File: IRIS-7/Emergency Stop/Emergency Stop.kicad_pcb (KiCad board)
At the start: 2 copper layers, 40 x 50 mm, 36 parts, among them IC1 LMR16006, J1 5mm TB, J2 ESTOP, J3 Pwr, J4 5mm TB, Q1 BSS123, Q2 BSS123, Q3 DMP3099L

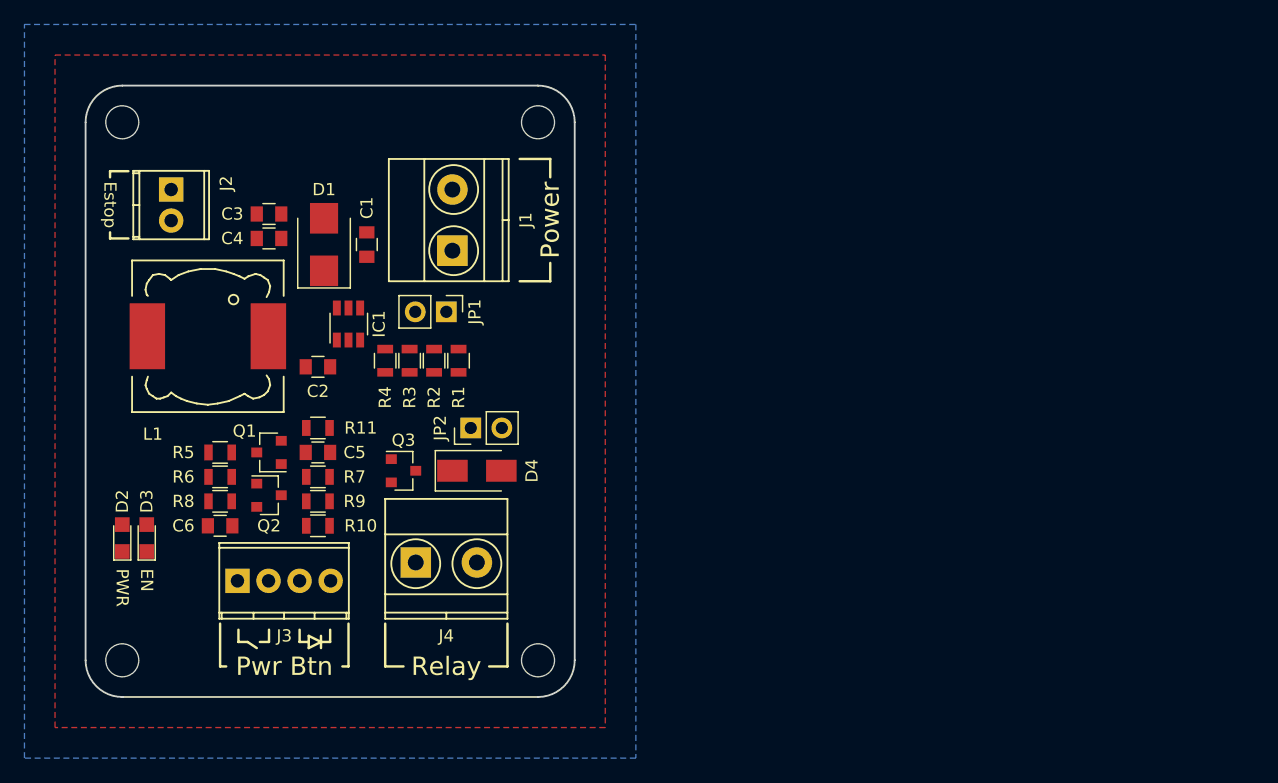
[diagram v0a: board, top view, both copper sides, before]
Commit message: Complete most of the routing
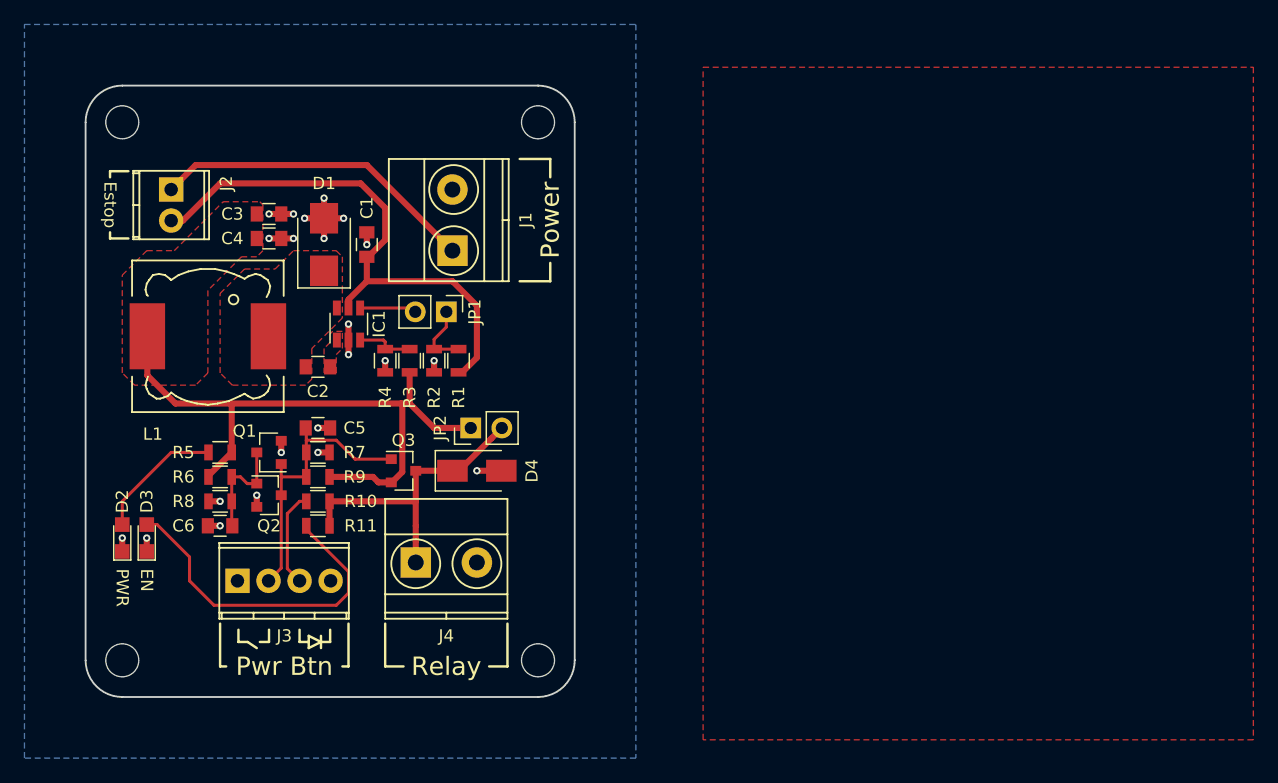
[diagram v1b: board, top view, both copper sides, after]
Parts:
- moved R11 8.00 mm to (119.0, 86.0)
- moved C5 2.00 mm to (119.0, 78.0)
- moved R10 2.00 mm to (119.0, 84.0)
- moved R7 2.00 mm to (119.0, 80.0)
- moved R9 2.00 mm to (119.0, 82.0)
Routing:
- net +12V: track 0.00 -> 54.0 mm
- net /Vin: track 0.00 -> 45.2 mm
- net Net-(D3-Pad2): track 0.00 -> 27.7 mm
- net /Vbatt: track 0.00 -> 26.7 mm
- net GND: track 0.00 -> 25.9 mm, vias 0 -> 22
- net /12Vout: track 0.00 -> 25.0 mm
- net /~EN: track 0.00 -> 23.7 mm
- net Net-(D2-Pad2): track 0.00 -> 10.6 mm
- net Net-(J3-Pad3): track 0.00 -> 8.96 mm
- net /EN: track 0.00 -> 8.85 mm
- net /UVLO: track 0.00 -> 5.46 mm
- net /FB: track 0.00 -> 4.71 mm
- net /~SHDN: track 0.00 -> 4.64 mm
- added copper zone on F.Cu, net +12V
- added copper zone on F.Cu, net /BOOT
- added copper zone on F.Cu, net /SW

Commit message: Clean up copper zones
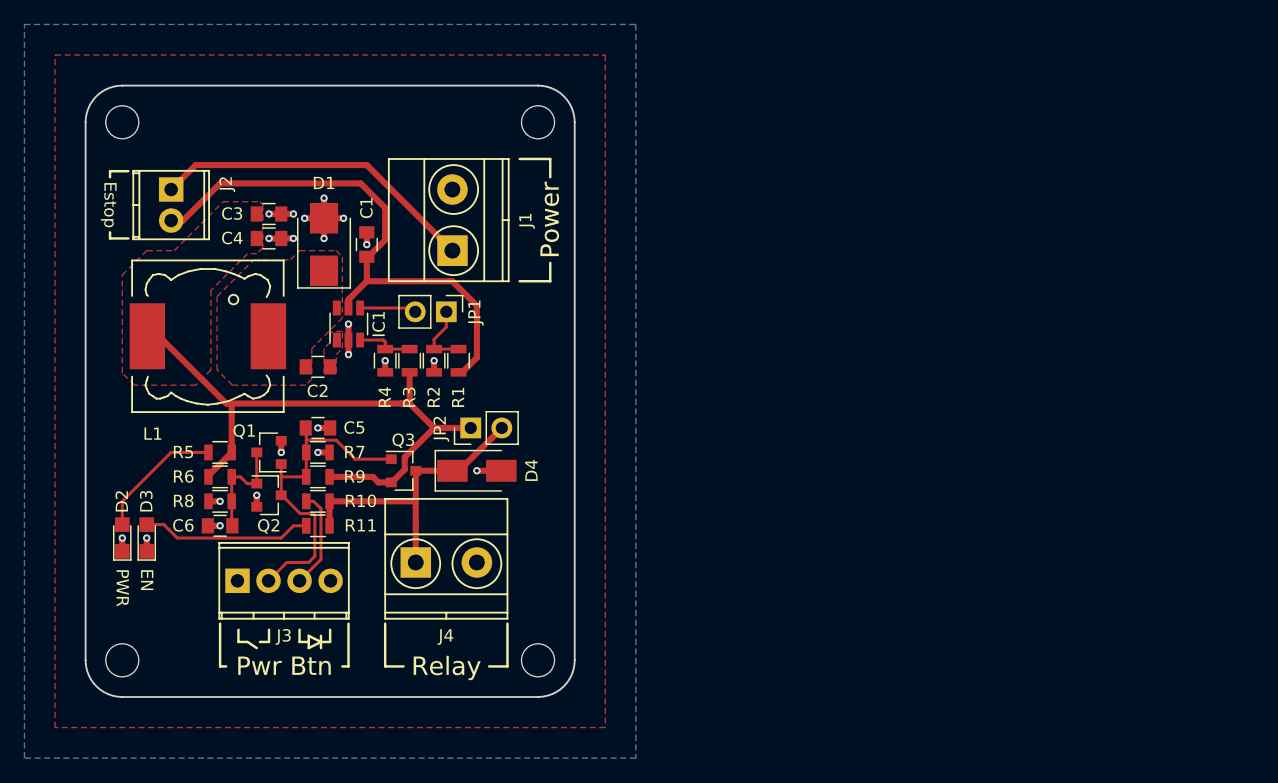
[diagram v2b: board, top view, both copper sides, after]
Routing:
- net Net-(D3-Pad2): track 27.7 -> 14.2 mm
- net /~EN: track 23.7 -> 27.6 mm
- net +12V: track 54.0 -> 51.1 mm
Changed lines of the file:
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@@
   (general
     (links 58)
-    (no_connects 48)
+    (no_connects 0)
     (area 99.924999 49.924999 140.075001 100.075001)
     (thickness 1.6)
     (drawings 43)
-    (tracks 140)
+    (tracks 142)
     (zones 0)
     (modules 36)
@@
   (layers
     (0 F.Cu signal)
-    (31 B.Cu signal hide)
+    (31 B.Cu signal)
     (32 B.Adhes user)
     (33 F.Adhes user hide)
@@
     (trace_clearance 0.2)
     (zone_clearance 0.254)
-    (zone_45_only no)
+    (zone_45_only yes)
     (trace_min 0.2)
     (segment_width 0.2)
@@
   (segment (start 119.95 80) (end 119 80) (width 0.5) (layer F.Cu) (net 1))
   (via (at 119 80) (size 0.6) (drill 0.3) (layers F.Cu B.Cu) (net 1))
+  (segment (start 125 82.45) (end 125.05 82.45) (width 0.5) (layer F.Cu) (net 4))
+  (segment (start 125.05 82.45) (end 126.099999 81.400001) (width 0.5) (layer F.Cu) (net 4))
+  (segment (start 126.099999 81.400001) (end 126.099999 80.400001) (width 0.5) (layer F.Cu) (net 4))
+  (segment (start 126.099999 80.400001) (end 128.5 78) (width 0.5) (layer F.Cu) (net 4))
+  (segment (start 105.04954 70.5) (end 106 70.5) (width 0.5) (layer F.Cu) (net 4))
+  (segment (start 106 70.5) (end 111.5 76) (width 0.5) (layer F.Cu) (net 4))
+  (segment (start 111.5 76) (end 111.89 76) (width 0.5) (layer F.Cu) (net 4))
   (segment (start 125 82.45) (end 123.95 82.45) (width 0.5) (layer F.Cu) (net 4))
   (segment (start 123.95 82.45) (end 123.5 82) (width 0.5) (layer F.Cu) (net 4))
   (segment (start 123.5 82) (end 119.95 82) (width 0.5) (layer F.Cu) (net 4))
-  (segment (start 107.34952 76) (end 111.89 76) (width 0.5) (layer F.Cu) (net 4))
   (segment (start 111.89 76) (end 125.81 76) (width 0.5) (layer F.Cu) (net 4))
   (segment (start 111.95 80) (end 111.95 76.06) (width 0.5) (layer F.Cu) (net 4))
   (segment (start 111.95 76.06) (end 111.89 76) (width 0.5) (layer F.Cu) (net 4))
   (segment (start 125.81 76) (end 126.5 76) (width 0.5) (layer F.Cu) (net 4))
-  (segment (start 125 82.45) (end 125.05 82.45) (width 0.5) (layer F.Cu) (net 4))
-  (segment (start 125.05 82.45) (end 125.900001 81.599999) (width 0.5) (layer F.Cu) (net 4))
-  (segment (start 125.900001 81.599999) (end 125.900001 76.090001) (width 0.5) (layer F.Cu) (net 4))
-  (segment (start 125.900001 76.090001) (end 125.81 76) (width 0.5) (layer F.Cu) (net 4))
   (segment (start 126.5 76) (end 128.5 78) (width 0.5) (layer F.Cu) (net 4))
   (segment (start 128.5 78) (end 131.5 78) (width 0.5) (layer F.Cu) (net 4))
-  (segment (start 105.04954 70.5) (end 105.04954 73.70002) (width 0.5) (layer F.Cu) (net 4))
-  (segment (start 105.04954 73.70002) (end 107.34952 76) (width 0.5) (layer F.Cu) (net 4))
   (segment (start 105.04954 70.5) (end 105.04954 71.54954) (width 0.5) (layer F.Cu) (net 4))
   (segment (start 126.5 73.45) (end 126.5 76) (width 0.5) (layer F.Cu) (net 4))
   (segment (start 110.05 82) (end 110.05 81.9) (width 0.5) (layer F.Cu) (net 4))
   (segment (start 110.05 81.9) (end 111.95 80) (width 0.5) (layer F.Cu) (net 4))
+  (segment (start 116 83.5) (end 116.05 83.5) (width 0.25) (layer F.Cu) (net 5))
+  (segment (start 116.05 83.5) (end 117.55 85) (width 0.25) (layer F.Cu) (net 5))
+  (segment (start 117.55 85) (end 118.61 85) (width 0.25) (layer F.Cu) (net 5))
+  (segment (start 118.61 85) (end 118.75 85.14) (width 0.25) (layer F.Cu) (net 5))
+  (segment (start 118.75 85.14) (end 118.75 88.5) (width 0.25) (layer F.Cu) (net 5))
+  (segment (start 118.75 88.5) (end 118.25 89) (width 0.25) (layer F.Cu) (net 5))
+  (segment (start 118.25 89) (end 116.46 89) (width 0.25) (layer F.Cu) (net 5))
+  (segment (start 116.46 89) (end 114.96 90.5) (width 0.25) (layer F.Cu) (net 5))
   (segment (start 118.05 82) (end 116 82) (width 0.25) (layer F.Cu) (net 5))
   (segment (start 118.05 79) (end 120.5 79) (width 0.25) (layer F.Cu) (net 5))
@@
   (segment (start 118.05 79) (end 118.05 78.05) (width 0.25) (layer F.Cu) (net 5))
   (segment (start 118.05 80) (end 118.05 79) (width 0.25) (layer F.Cu) (net 5))
-  (segment (start 116 83.5) (end 116 89.46) (width 0.25) (layer F.Cu) (net 5))
-  (segment (start 116 89.46) (end 114.96 90.5) (width 0.25) (layer F.Cu) (net 5))
   (segment (start 116 80.95) (end 116 82) (width 0.25) (layer F.Cu) (net 5))
   (segment (start 116 82) (end 116 83.5) (width 0.25) (layer F.Cu) (net 5))
-  (segment (start 116 83.5) (end 116.05 83.5) (width 0.25) (layer F.Cu) (net 5))
   (segment (start 118.05 78.05) (end 118 78) (width 0.25) (layer F.Cu) (net 5))
   (segment (start 118.05 82) (end 118.05 80) (width 0.25) (layer F.Cu) (net 5))
@@
   (segment (start 107 80) (end 103 84) (width 0.25) (layer F.Cu) (net 7))
   (segment (start 103 84) (end 103 85.9) (width 0.25) (layer F.Cu) (net 7))
+  (segment (start 118.05 86) (end 117 86) (width 0.25) (layer F.Cu) (net 8))
+  (segment (start 117 86) (end 116 87) (width 0.25) (layer F.Cu) (net 8))
+  (segment (start 116 87) (end 107.5 87) (width 0.25) (layer F.Cu) (net 8))
+  (segment (start 107.5 87) (end 106.4 85.9) (width 0.25) (layer F.Cu) (net 8))
+  (segment (start 106.4 85.9) (end 105 85.9) (width 0.25) (layer F.Cu) (net 8))
   (segment (start 118.05 86.3) (end 118.05 86) (width 0.25) (layer F.Cu) (net 8))
-  (segment (start 121.5 89.75) (end 118.05 86.3) (width 0.25) (layer F.Cu) (net 8))
-  (segment (start 121.5 91.5) (end 121.5 89.75) (width 0.25) (layer F.Cu) (net 8))
-  (segment (start 120.5 92.5) (end 121.5 91.5) (width 0.25) (layer F.Cu) (net 8))
-  (segment (start 110.5 92.5) (end 120.5 92.5) (width 0.25) (layer F.Cu) (net 8))
-  (segment (start 108.5 90.5) (end 110.5 92.5) (width 0.25) (layer F.Cu) (net 8))
-  (segment (start 108.5 88.55) (end 108.5 90.5) (width 0.25) (layer F.Cu) (net 8))
-  (segment (start 105.85 85.9) (end 108.5 88.55) (width 0.25) (layer F.Cu) (net 8))
-  (segment (start 105 85.9) (end 105.85 85.9) (width 0.25) (layer F.Cu) (net 8))
   (segment (start 119.95 86) (end 119.95 84) (width 0.5) (layer F.Cu) (net 9))
   (segment (start 127 86) (end 127 84) (width 0.5) (layer F.Cu) (net 9))
@@
   (segment (start 124.5 70.95) (end 124.5 71.55) (width 0.25) (layer F.Cu) (net 10))
   (segment (start 124.5 71.55) (end 126.5 71.55) (width 0.25) (layer F.Cu) (net 10))
-  (segment (start 118.05 84) (end 117.5 84) (width 0.25) (layer F.Cu) (net 11))
-  (segment (start 117.5 84) (end 116.5 85) (width 0.25) (layer F.Cu) (net 11))
-  (segment (start 116.5 85) (end 116.5 89.5) (width 0.25) (layer F.Cu) (net 11))
-  (segment (start 116.5 89.5) (end 117.5 90.5) (width 0.25) (layer F.Cu) (net 11))
-  (segment (start 118.05 84) (end 118.05 84.3) (width 0.25) (layer F.Cu) (net 11))
+  (segment (start 118.05 84) (end 118.65 84) (width 0.25) (layer F.Cu) (net 11))
+  (segment (start 118.65 84) (end 119.25 84.6) (width 0.25) (layer F.Cu) (net 11))
+  (segment (start 119.25 84.6) (end 119.25 88.75) (width 0.25) (layer F.Cu) (net 11))
+  (segment (start 119.25 88.75) (end 118.499489 89.500511) (width 0.25) (layer F.Cu) (net 11))
+  (segment (start 118.499489 89.500511) (end 117.5 90.5) (width 0.25) (layer F.Cu) (net 11))
   (segment (start 118.05 89.95) (end 117.5 90.5) (width 0.25) (layer F.Cu) (net 11))
   (segment (start 122.45 68.19) (end 126.65 68.19) (width 0.25) (layer F.Cu) (net 12))
@@
     (connect_pads (clearance 0.254))
     (min_thickness 0.254)
-    (fill yes (arc_segments 16) (thermal_gap 0.254) (thermal_bridge_width 0.508))
+    (fill yes (arc_segments 16) (thermal_gap 0.2) (thermal_bridge_width 0.508))
     (polygon
       (pts
-        (xy 150.5 48.5) (xy 195.5 48.5) (xy 195.5 103.5) (xy 150.5 103.5)
+        (xy 97.5 47.5) (xy 142.5 47.5) (xy 142.5 102.5) (xy 97.5 102.5)
       )
     )
   )
   (zone (net 3) (net_name /SW) (layer F.Cu) (hatch edge 0.508)
+    (priority 1)
     (connect_pads yes (clearance 0.254))
     (min_thickness 0.254)
@@
     (polygon
       (pts
-        (xy 113 65) (xy 115.5 65) (xy 117 63.5) (xy 120.5 63.5) (xy 121 64)
+        (xy 113.75 64.25) (xy 116.75 64.25) (xy 117.5 63.5) (xy 120.5 63.5) (xy 121 64)
         (xy 121 66.5) (xy 121 69) (xy 118.5 71.5) (xy 118.5 74) (xy 118 74.5)
-        (xy 112 74.5) (xy 111 73.5) (xy 111 67)
+        (xy 112 74.5) (xy 110.75 73.25) (xy 110.75 67.25)
       )
     )
@@
   )
   (zone (net 4) (net_name +12V) (layer F.Cu) (hatch edge 0.508)
+    (priority 1)
     (connect_pads yes (clearance 0.254))
     (min_thickness 0.254)
@@
     (polygon
       (pts
-        (xy 114.5 59.75) (xy 114.5 63.5) (xy 114 64) (xy 112.75 64) (xy 110 66.75)
-        (xy 110 73.5) (xy 109 74.5) (xy 104 74.5) (xy 103 73.5) (xy 103 65.5)
+        (xy 114.5 59.75) (xy 114.5 63.25) (xy 114 63.75) (xy 113.25 63.75) (xy 110.25 66.75)
+        (xy 110.25 73.25) (xy 109 74.5) (xy 104 74.5) (xy 103 73.5) (xy 103 65.5)
         (xy 105 63.5) (xy 107.25 63.5) (xy 111.25 59.5) (xy 114.25 59.5)
       )
